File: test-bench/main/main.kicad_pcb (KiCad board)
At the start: 2 copper layers, 35 parts, among them IC1 ATMEGA128-A, U1 4511N_DIL16, U2 LM2596S_TO263-5, U3 PCF8563, Y1 32khz

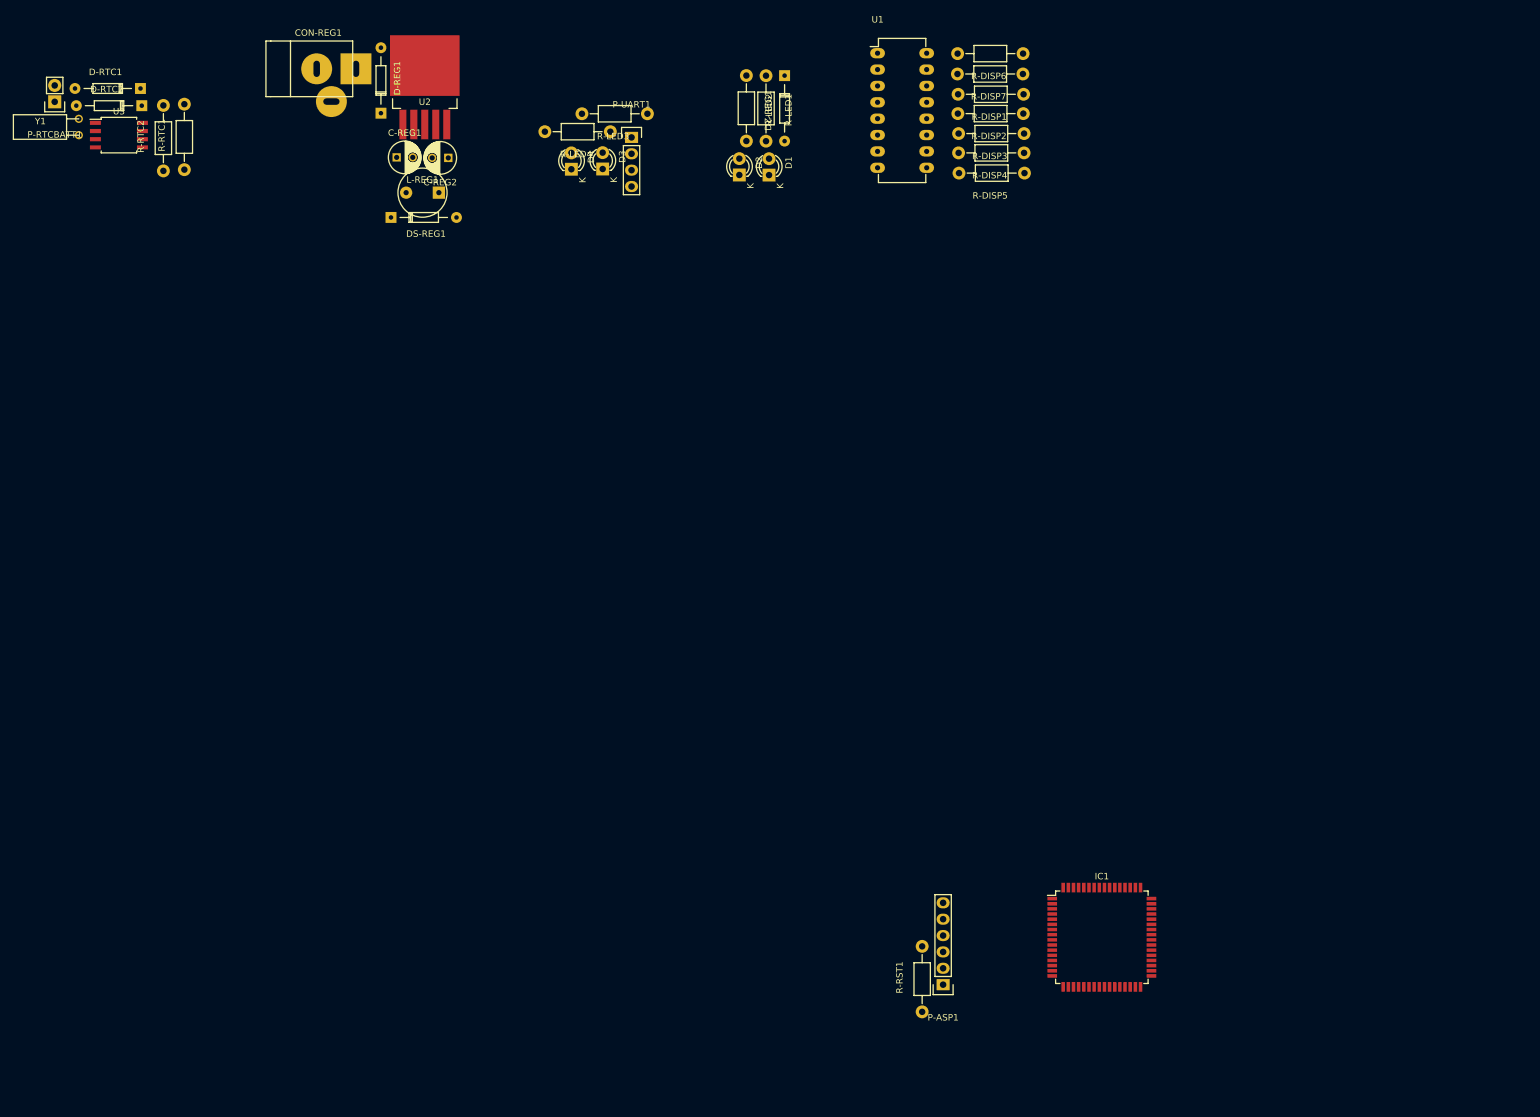
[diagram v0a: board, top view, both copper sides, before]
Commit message: Display Main Controller
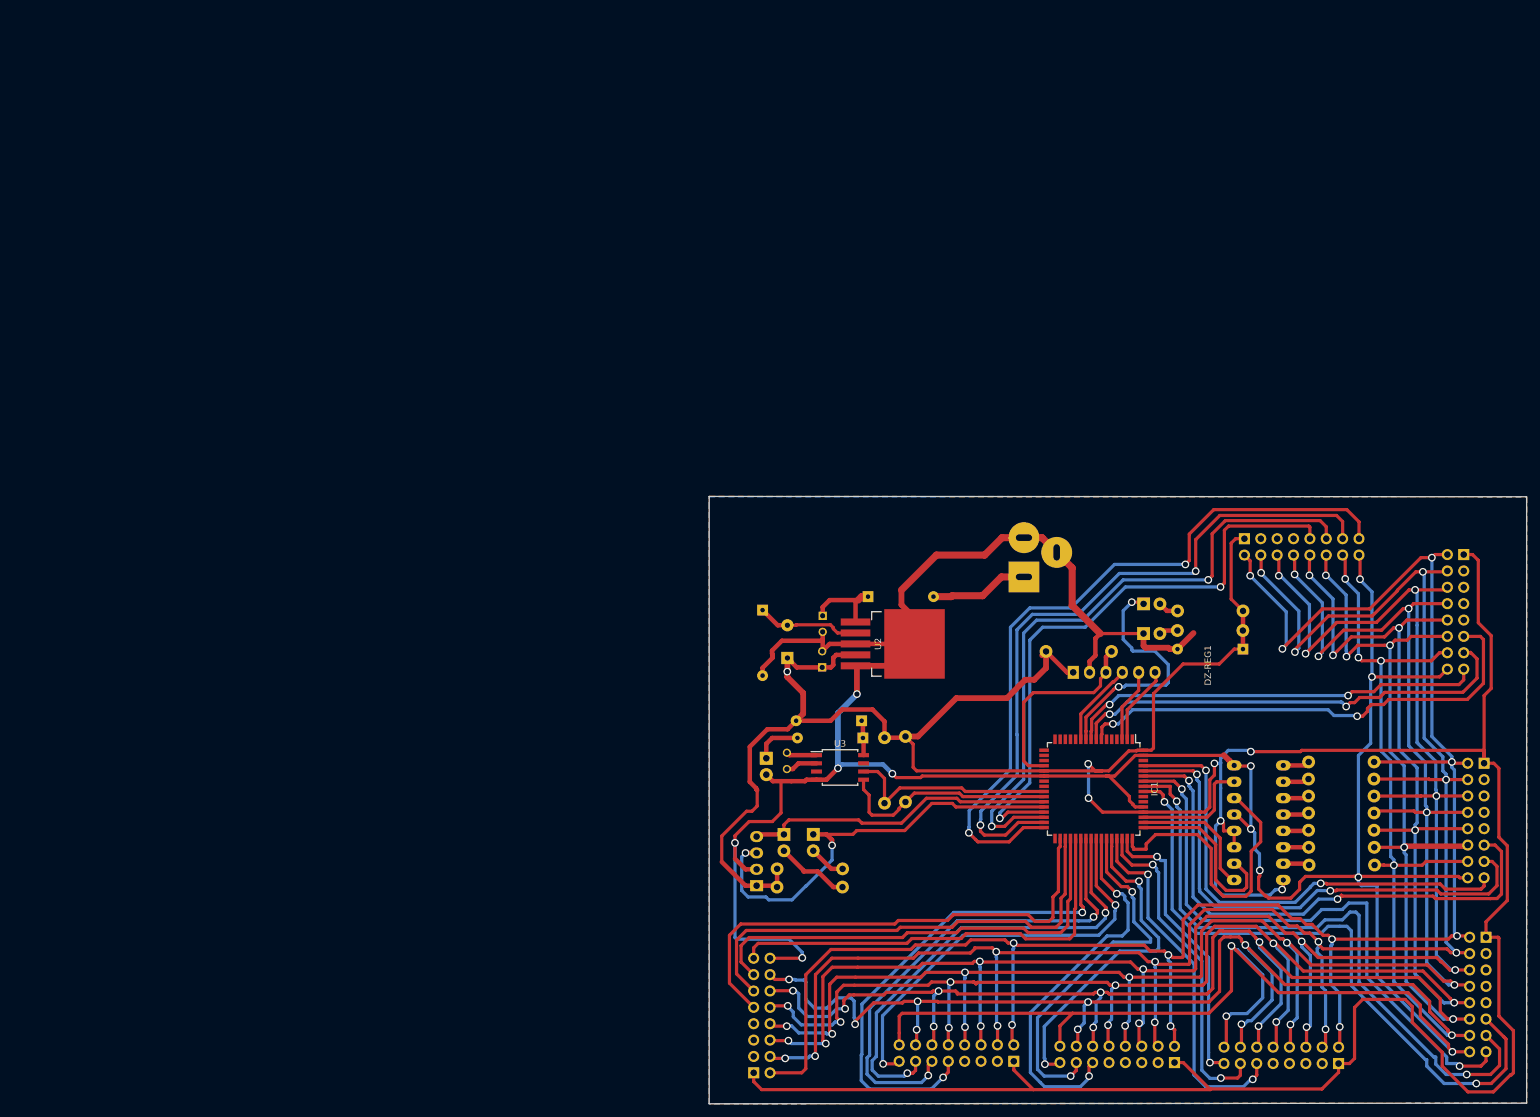
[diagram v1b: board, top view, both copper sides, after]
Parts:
- added P-LAMP1: CONN_02X08, Pin_Headers:Pin_Header_Straight_2x08, B.Cu at (211.3, 77.5)
- added P-LAMP2: CONN_02X08, Pin_Headers:Pin_Header_Straight_2x08, B.Cu at (211.6, 104.5)
- added P-LAMP3: CONN_02X08, Pin_Headers:Pin_Header_Straight_2x08, B.Cu at (208.1, 45.1)
- added P-LAMP4: CONN_02X08, Pin_Headers:Pin_Header_Straight_2x08, B.Cu at (188.7, 124.1)
- added P-LAMP5: CONN_02X08, Pin_Headers:Pin_Header_Straight_2x08, B.Cu at (163.3, 124.0)
- added P-LAMP6: CONN_02X08, Pin_Headers:Pin_Header_Straight_2x08, B.Cu at (138.3, 123.8)
- added P-LAMP7: CONN_02X08, Pin_Headers:Pin_Header_Straight_2x08, B.Cu at (98.0, 125.5)
- added P-LAMP8: CONN_02X08, Pin_Headers:Pin_Header_Straight_2x08, B.Cu at (174.1, 42.7)
- C-REG1, C-REG2, CON-REG1, D-REG1, D-RTC1, D-RTC2, D1, D2, D3, D4, DS-REG1, DZ-REG1, L-REG1, P-ASP1, P-RTCBATT1, P-UART1, R-DISP1, R-DISP2, R-DISP3, R-DISP4, R-DISP5, R-DISP6, R-DISP7, R-LED1, R-LED2, R-LED3, R-LED4, R-RST1, R-RTC1, R-RTC2, U1, Y1: moved to B.Cu
- moved P-RTCBATT1 150.2 mm to (99.9, 76.7)
- moved D-RTC1 148.8 mm to (114.7, 70.9)
- moved D-RTC2 148.8 mm to (114.9, 73.6)
- moved R-RTC1 148.8 mm to (121.5, 78.4), turned to 270 degrees
- moved R-RTC2 148.8 mm to (118.3, 78.6), turned to 270 degrees
- moved U3 148.8 mm to (111.4, 78.2)
- moved Y1 147.5 mm to (103.1, 77.1)
- moved U1 139.7 mm to (172.5, 95.6)
- moved R-DISP6 137.2 mm to (189.2, 93.3)
- moved R-DISP7 131.8 mm to (189.2, 90.5)
- moved CON-REG1 131.7 mm to (139.9, 42.5), turned to 270 degrees
- moved R-DISP1 126.5 mm to (189.1, 87.9)
- moved R-LED4 122.6 mm to (106.7, 96.7), turned to 0 degrees
- moved R-DISP2 121.4 mm to (189.1, 85.2)
- moved R-LED3 121.0 mm to (106.7, 93.9), turned to 0 degrees
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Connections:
- IC1 pad 29: Net-(IC1-Pad29) -> /D8-A
- IC1 pad 30: Net-(IC1-Pad30) -> /D8-B
- IC1 pad 31: Net-(IC1-Pad31) -> /D8-C
- IC1 pad 32: Net-(IC1-Pad32) -> /D8-D
- IC1 pad 34: Net-(IC1-Pad34) -> /D7-D
- IC1 pad 35: Net-(IC1-Pad35) -> /D7-C
- IC1 pad 36: Net-(IC1-Pad36) -> /D7-B
- IC1 pad 37: Net-(IC1-Pad37) -> /D7-A
- IC1 pad 38: Net-(IC1-Pad38) -> /D6-D
- IC1 pad 39: Net-(IC1-Pad39) -> /D6-C
- IC1 pad 40: Net-(IC1-Pad40) -> /D6-B
- IC1 pad 41: Net-(IC1-Pad41) -> /D6-A
- IC1 pad 42: Net-(IC1-Pad42) -> /D5-C
- IC1 pad 43: Net-(IC1-Pad43) -> /D5-B
- IC1 pad 44: Net-(IC1-Pad44) -> /D5-A
- IC1 pad 45: Net-(IC1-Pad45) -> /D4-C
- IC1 pad 46: Net-(IC1-Pad46) -> /D4-B
- IC1 pad 47: Net-(IC1-Pad47) -> /D4-A
- IC1 pad 56: Net-(IC1-Pad56) -> /D2-C
- IC1 pad 57: Net-(IC1-Pad57) -> /D2-B
- IC1 pad 58: Net-(IC1-Pad58) -> /D2-A
- IC1 pad 59: Net-(IC1-Pad59) -> /D1-C
- IC1 pad 60: Net-(IC1-Pad60) -> /D1-B
- IC1 pad 61: Net-(IC1-Pad61) -> /D1-A
- IC1 pad 7: Net-(IC1-Pad7) -> /D3-A
- IC1 pad 8: Net-(IC1-Pad8) -> /D3-B
- IC1 pad 9: Net-(IC1-Pad9) -> /D3-C
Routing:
- net VCC: track 0.00 -> 575.2 mm, vias 0 -> 7
- net GND: track 0.00 -> 575.1 mm, vias 0 -> 14
- net /LE: track 0.00 -> 308.4 mm, vias 0 -> 11
- net /LD: track 0.00 -> 302.6 mm, vias 0 -> 13
- net /LC: track 0.00 -> 296.2 mm, vias 0 -> 13
- net /LG: track 0.00 -> 289.3 mm, vias 0 -> 13
- net /LB: track 0.00 -> 288.4 mm, vias 0 -> 13
- net /LA: track 0.00 -> 282.9 mm, vias 0 -> 13
- net /LF: track 0.00 -> 278.7 mm, vias 0 -> 13
- net /D8-D: track 0.00 -> 115.3 mm, vias 0 -> 2
- net /D8-C: track 0.00 -> 108.4 mm, vias 0 -> 2
- net /D2-C: track 0.00 -> 101.1 mm, vias 0 -> 2
- net /D8-B: track 0.00 -> 101.0 mm, vias 0 -> 2
- net /D2-B: track 0.00 -> 98.9 mm, vias 0 -> 2
- net /D8-A: track 0.00 -> 94.3 mm, vias 0 -> 2
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- added copper zone on B.Cu, net (none)
- added copper zone on F.Cu, net (none)
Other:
- board outline added: 126.9 x 94.2 mm

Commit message: lapooor
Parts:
- added REF**: MountingHole_2-5mm, Mounting_Holes:MountingHole_2-5mm, F.Cu at (218.3, 129.0)
- added REF**: MountingHole_2-5mm, Mounting_Holes:MountingHole_2-5mm, F.Cu at (218.2, 38.1)
- added REF**: MountingHole_2-5mm, Mounting_Holes:MountingHole_2-5mm, F.Cu at (91.2, 38.1)
- added REF**: MountingHole_2-5mm, Mounting_Holes:MountingHole_2-5mm, F.Cu at (91.2, 129.0)
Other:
- board size 126.9 x 94.2 mm -> 133.7 x 97 mm
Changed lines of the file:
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@@
 (kicad_pcb (version 4) (host pcbnew "(2015-11-24 BZR 6329, Git e511afd)-product")
   (general
-    (links 175)
-    (no_connects 4)
-    (area 92.457099 32.168809 216.708334 131.615)
+    (links 0)
+    (no_connects 1)
+    (area 90.974999 32.168809 217.975001 131.615)
     (thickness 1.6)
     (drawings 4)
     (tracks 1756)
     (zones 0)
-    (modules 43)
+    (modules 47)
     (nets 117)
   )
@@
   )
   (setup
-    (last_trace_width 1.1)
+    (last_trace_width 0.25)
     (user_trace_width 0.4)
     (user_trace_width 0.5)
@@
     )
   )
-  (gr_line (start 91.05 130.35) (end 91.05 36.1) (layer Edge.Cuts) (width 0.15))
-  (gr_line (start 217.9 130.25) (end 91.05 130.35) (layer Edge.Cuts) (width 0.15))
-  (gr_line (start 217.9 36.15) (end 217.9 130.25) (layer Edge.Cuts) (width 0.15))
-  (gr_line (start 91.05 36.1) (end 217.9 36.15) (layer Edge.Cuts) (width 0.15))
+  (module Mounting_Holes:MountingHole_2-5mm (layer F.Cu)
+    (at 218.3 129)
+    (descr "Mounting hole, Befestigungsbohrung, 2,5mm, No Annular, Kein Restring,")
+    (tags "Mounting hole, Befestigungsbohrung, 2,5mm, No Annular, Kein Restring,")
+    (fp_text reference REF** (at 0 -3.50012) (layer F.SilkS)
+      (effects (font (size 1 1) (thickness 0.15)))
+    )
+    (fp_text value MountingHole_2-5mm (at 0.09906 3.59918) (layer F.Fab)
+      (effects (font (size 1 1) (thickness 0.15)))
+    )
+    (fp_circle (center 0 0) (end 2.5 0) (layer Cmts.User) (width 0.381))
+    (pad 1 thru_hole circle (at 0 0) (size 2.5 2.5) (drill 2.5) (layers))
+  )
+  (module Mounting_Holes:MountingHole_2-5mm (layer F.Cu)
+    (at 218.2 38.1)
+    (descr "Mounting hole, Befestigungsbohrung, 2,5mm, No Annular, Kein Restring,")
+    (tags "Mounting hole, Befestigungsbohrung, 2,5mm, No Annular, Kein Restring,")
+    (fp_text reference REF** (at 0 -3.50012) (layer F.SilkS)
+      (effects (font (size 1 1) (thickness 0.15)))
+    )
+    (fp_text value MountingHole_2-5mm (at 0.09906 3.59918) (layer F.Fab)
+      (effects (font (size 1 1) (thickness 0.15)))
+    )
+    (fp_circle (center 0 0) (end 2.5 0) (layer Cmts.User) (width 0.381))
+    (pad 1 thru_hole circle (at 0 0) (size 2.5 2.5) (drill 2.5) (layers))
+  )
+  (module Mounting_Holes:MountingHole_2-5mm (layer F.Cu)
+    (at 91.2 38.1)
+    (descr "Mounting hole, Befestigungsbohrung, 2,5mm, No Annular, Kein Restring,")
+    (tags "Mounting hole, Befestigungsbohrung, 2,5mm, No Annular, Kein Restring,")
+    (fp_text reference REF** (at 0 -3.50012) (layer F.SilkS)
+      (effects (font (size 1 1) (thickness 0.15)))
+    )
+    (fp_text value MountingHole_2-5mm (at 0.09906 3.59918) (layer F.Fab)
+      (effects (font (size 1 1) (thickness 0.15)))
+    )
+    (fp_circle (center 0 0) (end 2.5 0) (layer Cmts.User) (width 0.381))
+    (pad 1 thru_hole circle (at 0 0) (size 2.5 2.5) (drill 2.5) (layers))
+  )
+  (module Mounting_Holes:MountingHole_2-5mm (layer F.Cu)
+    (at 91.2 129)
+    (descr "Mounting hole, Befestigungsbohrung, 2,5mm, No Annular, Kein Restring,")
+    (tags "Mounting hole, Befestigungsbohrung, 2,5mm, No Annular, Kein Restring,")
+    (fp_text reference REF** (at 0 -3.50012) (layer F.SilkS)
+      (effects (font (size 1 1) (thickness 0.15)))
+    )
+    (fp_text value MountingHole_2-5mm (at 0.09906 3.59918) (layer F.Fab)
+      (effects (font (size 1 1) (thickness 0.15)))
+    )
+    (fp_circle (center 0 0) (end 2.5 0) (layer Cmts.User) (width 0.381))
+    (pad 1 thru_hole circle (at 0 0) (size 2.5 2.5) (drill 2.5) (layers))
+  )
+  (gr_line (start 88.3 131.9) (end 88.1 35) (layer Edge.Cuts) (width 0.15))
+  (gr_line (start 221.8 132) (end 88.3 131.9) (layer Edge.Cuts) (width 0.15))
+  (gr_line (start 221.6 35.1) (end 221.8 132) (layer Edge.Cuts) (width 0.15))
+  (gr_line (start 88.1 35) (end 221.6 35.1) (layer Edge.Cuts) (width 0.15))
   (segment (start 160.3875 64.75366) (end 160.3875 63.548998) (width 0.5) (layer F.Cu) (net 2))
   (segment (start 160.3875 63.548998) (end 160.241931 63.403429) (width 0.5) (layer F.Cu) (net 2))
@@
     (polygon
       (pts
-        (xy 91.05 36.1) (xy 217.9 36.15) (xy 217.9 130.25) (xy 91.05 130.35)
+        (xy 88.1 35) (xy 221.6 35.1) (xy 221.8 132) (xy 88.3 131.9)
       )
     )
@@
     (polygon
       (pts
-        (xy 91.05 36.15) (xy 217.9 36.15) (xy 217.9 130.25) (xy 91.05 130.35)
+        (xy 88.1 35) (xy 221.6 35.1) (xy 221.8 132) (xy 88.3 131.9)
       )
     )
